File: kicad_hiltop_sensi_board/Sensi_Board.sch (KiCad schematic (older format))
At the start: 98 parts, among them J1 Conn_02x06_Counter_Clockwise, J10 Conn_ARM_JTAG_SWD_10, J2 Conn_02x06_Counter_Clockwise, J3 Conn_03x32_DIN41612, J4 Conn_02x06_Counter_Clockwise, J5 Conn_02x06_Counter_Clockwise, J6 Conn_02x06_Counter_Clockwise, J7 Conn_02x06_Counter_Clockwise, J8 Conn_02x06_Counter_Clockwise, U1 INA250A4, U2 LD1117S33TR_SOT223, U3 AT25DN512CSSHF-B, U6 LM75B

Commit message: Updated sensi board pin map and layout before PCB tracking
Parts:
- C23, C24: Devtank (none) -> 105-019
- J1, J2, J4, J5, J6, J7, J8: Devtank (none) -> 711-004
- J10: Devtank (none) -> 710-020
- JP1: Devtank 710-015 -> 710-014
- R30, R32, R34: Devtank (none) -> 101-005
- R37, R38: Devtank (none) -> 101-010
- R39, R40: Devtank (none) -> 101-015
- R8, R9: Devtank 101-007 -> (none)
- U6: Devtank (none) -> 155-005
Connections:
- net ADC10: no longer J5.3 (Pin_3), TP56.1
- net ADC11: no longer J5.5 (Pin_5), TP57.1
- net ADC12: now also J5.5 (Pin_5), TP57.1; no longer J5.12 (Pin_12), TP58.1
- net ADC6: now also J5.12 (Pin_12), TP58.1
- net ADC7: now also J5.1 (Pin_1), TP55.1
- net ADC9: no longer J5.1 (Pin_1), TP55.1
- net STM_Micro/ADC13 renamed STM_Micro/ADC8
- new net ADC13: J5.3 (Pin_3), TP56.1
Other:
- moved on the sheet: R149
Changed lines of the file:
@@
 F 2 "Connector_PinHeader_2.54mm:PinHeader_1x03_P2.54mm_Vertical" H 18475 3825 50  0001 C CNN
 F 3 "" H 18475 3825 50  0001 C CNN
-F 4 "710-015" H 0   0   50  0001 C CNN "Devtank"
+F 4 "710-014" H 0   0   50  0001 C CNN "Devtank"
 	1    18475 3825
 	0    1    1    0
@@
 F 2 "Resistor_SMD:R_1206_3216Metric" V 17755 9150 50  0001 C CNN
 F 3 "" H 17825 9150 50  0001 C CNN
-F 4 "101-007" H -350 1050 50  0001 C CNN "Devtank"
+F 4 "" H -350 1050 50  0001 C CNN "Devtank"
 	1    17825 9150
 	-1   0    0    1
@@
 F 2 "Resistor_SMD:R_1206_3216Metric" V 17505 9150 50  0001 C CNN
 F 3 "" H 17575 9150 50  0001 C CNN
-F 4 "101-007" H -350 1050 50  0001 C CNN "Devtank"
+F 4 "" H -350 1050 50  0001 C CNN "Devtank"
 	1    17575 9150
 	-1   0    0    1
@@
 Wire Wire Line
 	3225 3725 2175 3725
-Wire Wire Line
-	3225 3850 2175 3850
 Text Label 2175 2975 0    60   ~ 0
 ADC1
@@
 Text Label 2175 3725 0    60   ~ 0
 ADC7
-Text Label 2175 3850 0    60   ~ 0
-ADC8
 Text Label 2175 3975 0    60   ~ 0
 ADC9
@@
 Wire Wire Line
 	21675 5250 21675 5175
-Text Label 950  4475 0    60   ~ 0
+Text Label 950  3850 0    60   ~ 0
 I_MON
 Text Label 20800 11050 2    60   ~ 0
@@
 L Sensi_Board-rescue:R-device R149
 U 1 1 5CC4B709
-P 1875 4475
-F 0 "R149" V 1825 4225 50  0000 C CNN
-F 1 "0R" V 1825 4700 50  0000 C CNN
-F 2 "Resistor_SMD:R_0603_1608Metric" V 1805 4475 50  0001 C CNN
-F 3 "" H 1875 4475 50  0001 C CNN
-F 4 "101-005" H 150 1150 50  0001 C CNN "Devtank"
-	1    1875 4475
+P 1875 3850
+F 0 "R149" V 1825 3600 50  0000 C CNN
+F 1 "0R" V 1825 4075 50  0000 C CNN
+F 2 "Resistor_SMD:R_0603_1608Metric" V 1805 3850 50  0001 C CNN
+F 3 "" H 1875 3850 50  0001 C CNN
+F 4 "101-005" H 150 525 50  0001 C CNN "Devtank"
+	1    1875 3850
 	0    1    1    0
 $EndComp
 Wire Wire Line
-	950  4475 1725 4475
+	950  3850 1725 3850
 Wire Wire Line
 	2175 3475 3225 3475
@@
 ADC12
 Wire Wire Line
-	2025 4475 3225 4475
+	2025 3850 3225 3850
 Text Label 13850 4525 0    60   ~ 0
 USB_DATA_N
@@
 Wire Wire Line
 	12525 7775 13025 7775
-Text Label 13025 7775 2    60   ~ 0
+Text Label 13025 6875 2    60   ~ 0
 ADC5
-Text Label 13025 7475 2    60   ~ 0
+Text Label 11025 14750 2    60   ~ 0
 ADC6
-Text Label 13025 7175 2    60   ~ 0
+Text Label 11025 14300 2    60   ~ 0
 ADC7
-Text Label 13025 6875 2    60   ~ 0
-ADC8
+Text Label 11050 14450 2    60   ~ 0
+ADC13
 Wire Wire Line
 	20900 5250 20425 5250
@@
 	20425 5150 20425 5250
 Connection ~ 20425 5250
-Text Label 8350 9450 2    60   ~ 0
+Text Label 13025 7175 2    60   ~ 0
 ADC4
-Text Label 8350 8850 2    60   ~ 0
+Text Label 13025 7475 2    60   ~ 0
 ADC3
-Text Label 8350 8550 2    60   ~ 0
+Text Label 13025 7775 2    60   ~ 0
 ADC2
 Text Label 8350 9150 2    60   ~ 0
@@
 Text Label 8675 14750 0    60   ~ 0
 5V_ADC12
-Text Label 11100 14750 2    60   ~ 0
+Text Label 11050 14600 2    60   ~ 0
 ADC12
 $Comp
@@
 F 2 "Package_SO:SOIC-8_3.9x4.9mm_P1.27mm" H 8300 11650 50  0001 C CNN
 F 3 "http://www.ti.com/lit/ds/symlink/lm75b.pdf" H 8300 11650 50  0001 C CNN
+F 4 "155-005" H 8300 11650 50  0001 C CNN "Devtank"
 	1    8300 11650
 	-1   0    0    -1
@@
 F 2 "Capacitor_SMD:C_0402_1005Metric" H 8738 10825 50  0001 C CNN
 F 3 "" H 8700 10975 50  0001 C CNN
+F 4 "105-019" H 8700 10975 50  0001 C CNN "Devtank"
 	1    8700 10975
 	0    -1   -1   0
@@
 F 2 "Resistor_SMD:R_0603_1608Metric" V 7305 11275 50  0001 C CNN
 F 3 "" H 7375 11275 50  0001 C CNN
+F 4 "101-005" H 7375 11275 50  0001 C CNN "Devtank"
 	1    7375 11275
 	1    0    0    -1
@@
 F 2 "Resistor_SMD:R_0603_1608Metric" V 7555 11275 50  0001 C CNN
 F 3 "" H 7625 11275 50  0001 C CNN
+F 4 "101-005" H 7625 11275 50  0001 C CNN "Devtank"
 	1    7625 11275
 	1    0    0    -1
@@
 F 2 "Resistor_SMD:R_0603_1608Metric" V 7055 11275 50  0001 C CNN
 F 3 "" H 7125 11275 50  0001 C CNN
+F 4 "101-005" H 7125 11275 50  0001 C CNN "Devtank"
 	1    7125 11275
 	1    0    0    -1
@@
 F 2 "Resistor_SMD:R_0603_1608Metric" V 5480 11300 50  0001 C CNN
 F 3 "" H 5550 11300 50  0001 C CNN
+F 4 "101-010" H 5550 11300 50  0001 C CNN "Devtank"
 	1    5550 11300
 	0    1    1    0
@@
 F 2 "Resistor_SMD:R_0603_1608Metric" V 5280 10650 50  0001 C CNN
 F 3 "" H 5350 10650 50  0001 C CNN
+F 4 "101-010" H 5350 10650 50  0001 C CNN "Devtank"
 	1    5350 10650
 	1    0    0    -1
@@
 F 2 "Connector_PinHeader_2.54mm:PinHeader_2x05_P2.54mm_Vertical" H 1750 7950 50  0001 L TNN
 F 3 "http://infocenter.arm.com/help/topic/com.arm.doc.faqs/attached/13634/cortex_debug_connectors.pdf" V 1350 7250 50  0001 C CNN
+F 4 "710-020" H 1700 8500 50  0001 C CNN "Devtank"
 	1    1700 8500
 	1    0    0    -1
@@
 F 2 "Capacitor_SMD:C_0402_1005Metric" H 988 8300 50  0001 C CNN
 F 3 "" H 950 8450 50  0001 C CNN
+F 4 "105-019" H 950 8450 50  0001 C CNN "Devtank"
 	1    950  8450
 	1    0    0    -1
@@
 F 2 "Resistor_SMD:R_0603_1608Metric" V 2880 8400 50  0001 C CNN
 F 3 "" H 2950 8400 50  0001 C CNN
+F 4 "101-015" H 2950 8400 50  0001 C CNN "Devtank"
 	1    2950 8400
 	0    -1   -1   0
@@
 F 2 "Resistor_SMD:R_0603_1608Metric" V 2880 8550 50  0001 C CNN
 F 3 "" H 2950 8550 50  0001 C CNN
+F 4 "101-015" H 2950 8550 50  0001 C CNN "Devtank"
 	1    2950 8550
 	0    -1   -1   0
@@
 F 2 "Devtank_PCB_Lib:Molex2x06" H 12750 10075 50  0001 C CNN
 F 3 "~" H 12750 10075 50  0001 C CNN
+F 4 "711-004" H 12750 10075 50  0001 C CNN "Devtank"
 	1    12750 10075
 	1    0    0    -1
@@
 F 2 "Devtank_PCB_Lib:Molex2x06" H 12725 11375 50  0001 C CNN
 F 3 "~" H 12725 11375 50  0001 C CNN
+F 4 "711-004" H 12725 11375 50  0001 C CNN "Devtank"
 	1    12725 11375
 	1    0    0    -1
@@
 F 2 "Devtank_PCB_Lib:Molex2x06" H 7150 14425 50  0001 C CNN
 F 3 "~" H 7150 14425 50  0001 C CNN
+F 4 "711-004" H 7150 14425 50  0001 C CNN "Devtank"
 	1    7150 14425
 	1    0    0    -1
@@
 	6950 14225 6525 14225
 Text Label 6525 14225 0    60   ~ 0
-ADC9
+ADC7
 Wire Wire Line
 	6950 14425 6525 14425
 Text Label 6525 14425 0    60   ~ 0
-ADC10
+ADC13
 Wire Wire Line
 	6950 14625 6525 14625
 Text Label 6525 14625 0    60   ~ 0
-ADC11
+ADC12
 Wire Wire Line
 	7450 14225 7875 14225
 Text Label 7875 14225 2    60   ~ 0
-ADC12
+ADC6
 NoConn ~ 7450 14525
 NoConn ~ 7450 14425
@@
 F 2 "Devtank_PCB_Lib:Molex2x06" H 10000 7300 50  0001 C CNN
 F 3 "~" H 10000 7300 50  0001 C CNN
+F 4 "711-004" H 10000 7300 50  0001 C CNN "Devtank"
 	1    10000 7300
 	1    0    0    -1
@@
 F 2 "Devtank_PCB_Lib:Molex2x06" H 4925 8950 50  0001 C CNN
 F 3 "~" H 4925 8950 50  0001 C CNN
+F 4 "711-004" H 4925 8950 50  0001 C CNN "Devtank"
 	1    4925 8950
 	1    0    0    -1
@@
 F 2 "Devtank_PCB_Lib:Molex2x06" H 4700 11200 50  0001 C CNN
 F 3 "~" H 4700 11200 50  0001 C CNN
+F 4 "711-004" H 4700 11200 50  0001 C CNN "Devtank"
 	1    4700 11200
 	1    0    0    -1
@@
 F 2 "Devtank_PCB_Lib:Molex2x06" H 1950 11325 50  0001 C CNN
 F 3 "~" H 1950 11325 50  0001 C CNN
+F 4 "711-004" H 1950 11325 50  0001 C CNN "Devtank"
 	1    1950 11325
 	1    0    0    -1
@@
 NoConn ~ 7450 14625
 NoConn ~ 7450 14725
-Text Label 11100 14600 2    60   ~ 0
+Text Label 8350 8550 2    60   ~ 0
 ADC11
-Text Label 11100 14450 2    60   ~ 0
+Text Label 8350 8850 2    60   ~ 0
 ADC10
-Text Label 11100 14300 2    60   ~ 0
+Text Label 8350 9450 2    60   ~ 0
 ADC9
 Wire Wire Line
@@
 NoConn ~ 2525 6775
 NoConn ~ 2525 6900
+Wire Wire Line
+	3225 4475 2175 4475
+Text Label 2175 4475 0    60   ~ 0
+ADC13
 $EndSCHEMATC

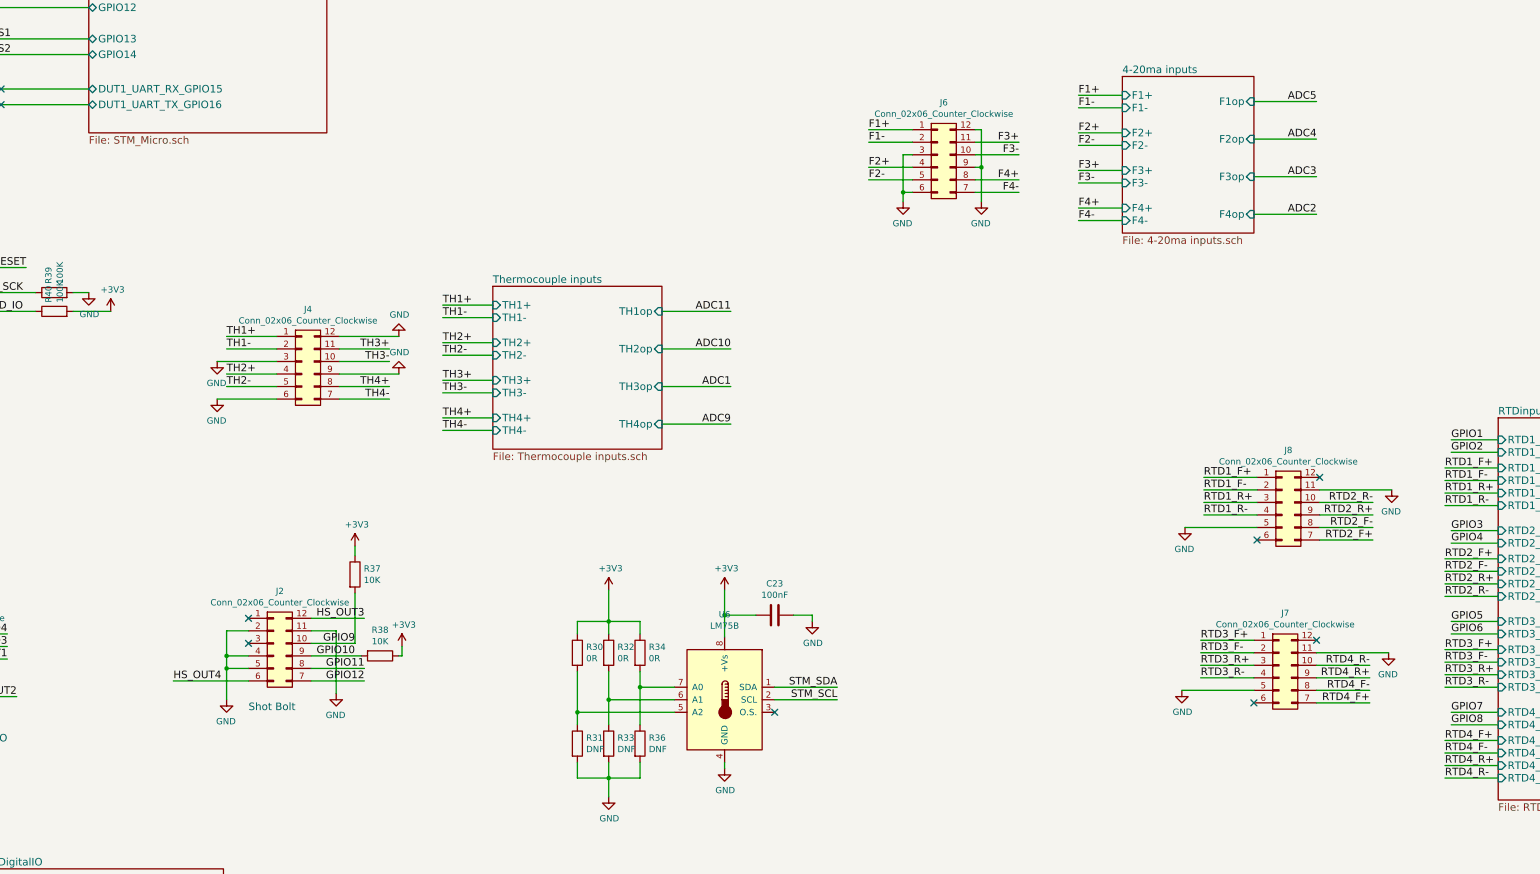
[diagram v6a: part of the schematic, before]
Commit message: Started PCB routing of Sensi Board LBBC
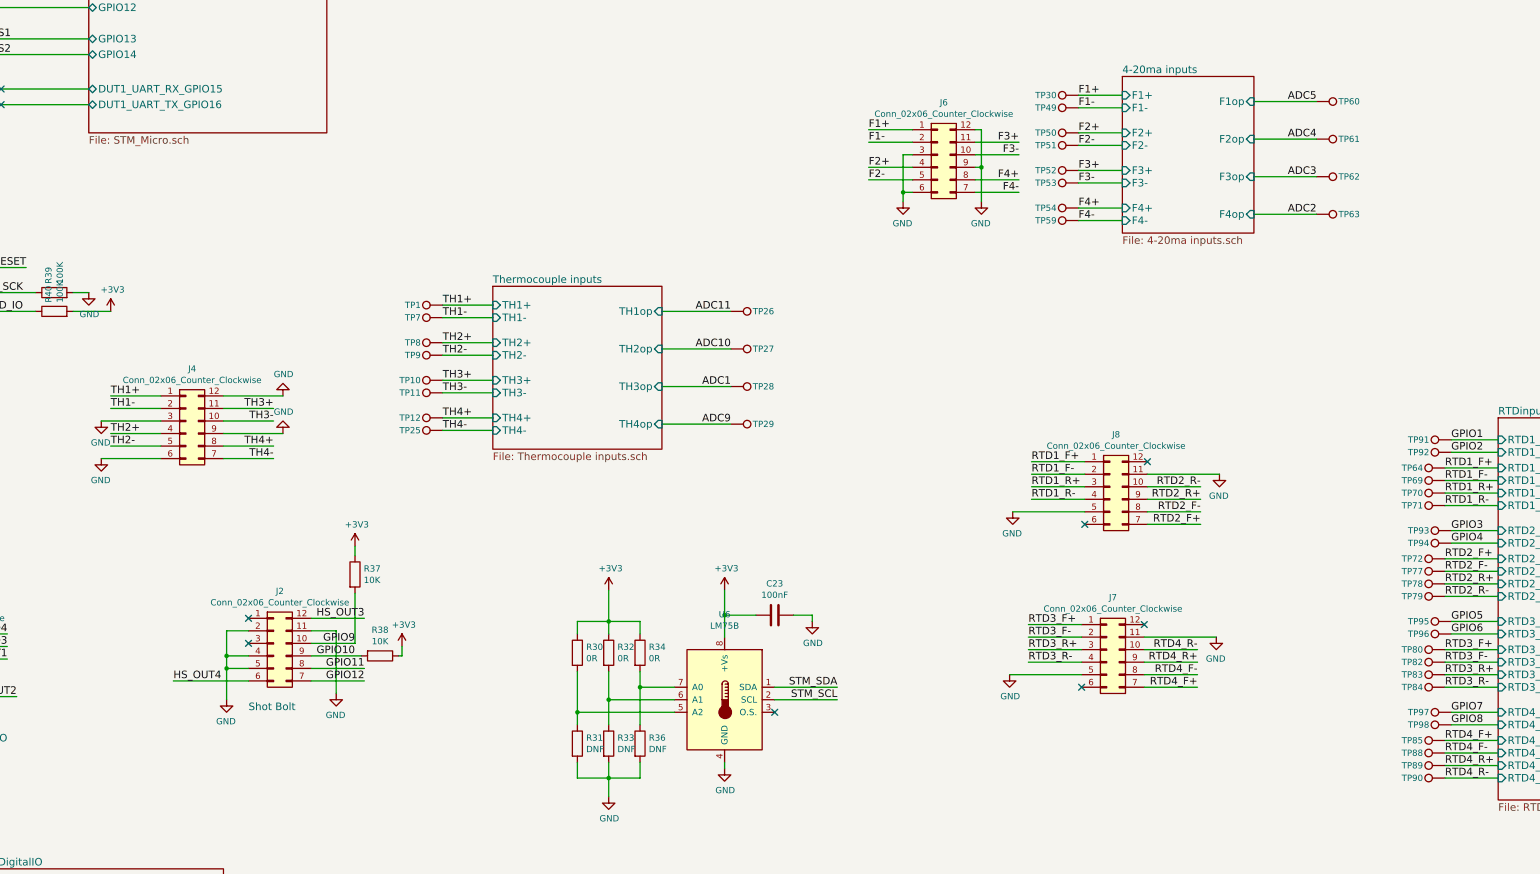
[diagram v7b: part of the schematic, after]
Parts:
- added TP1, TP10, TP11, TP12, TP25, TP26, TP27, TP28, TP29, TP30, TP49, TP50, TP51, TP52, TP53, TP54, TP59, TP60, TP61, TP62, TP63, TP64, TP69, TP7, TP70, TP71, TP72, TP77, TP78, TP79, TP8, TP80, TP82, TP83, TP84, TP85, TP88, TP89, TP9, TP90, TP91, TP92, TP93, TP94, TP95, TP96, TP97, TP98: Test_Point, TestPoint:TestPoint_THTPad_D1.0mm_Drill0.5mm, symbol Sensi_Board-rescue:Test_Point-Connector
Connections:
- net ADC1: now also TP28.1
- net ADC10: now also TP27.1
- net ADC11: now also TP26.1
- net ADC2: now also TP63.1
- net ADC3: now also TP62.1
- net ADC4: now also TP61.1
- net ADC5: now also TP60.1
- net ADC9: now also TP29.1
- net F1+: now also TP30.1
- net F1-: now also TP49.1
- net F2+: now also TP50.1
- net F2-: now also TP51.1
- net F3+: now also TP52.1
- net F3-: now also TP53.1
- net F4+: now also TP54.1
- net F4-: now also TP59.1
- net GPIO1: now also TP91.1
- net GPIO2: now also TP92.1
- net GPIO3: now also TP93.1
- net GPIO4: now also TP94.1
- net GPIO5: now also TP95.1
- net GPIO6: now also TP96.1
- net GPIO7: now also TP97.1
- net GPIO8: now also TP98.1
- net RTD1_F+: now also TP64.1
- net RTD1_F-: now also TP69.1
- net RTD1_R+: now also TP70.1
- net RTD1_R-: now also TP71.1
- net RTD2_F+: now also TP72.1
- net RTD2_F-: now also TP77.1
- net RTD2_R+: now also TP78.1
- net RTD2_R-: now also TP79.1
- net RTD3_F+: now also TP80.1
- net RTD3_F-: now also TP82.1
- net RTD3_R+: now also TP83.1
- net RTD3_R-: now also TP84.1
- net RTD4_F+: now also TP85.1
- net RTD4_F-: now also TP88.1
- net RTD4_R+: now also TP89.1
- net RTD4_R-: now also TP90.1
- net TH1+: now also TP1.1
- net TH1-: now also TP7.1
- net TH2+: now also TP8.1
- net TH2-: now also TP9.1
- net TH3+: now also TP10.1
- net TH3-: now also TP11.1
- net TH4+: now also TP12.1
- net TH4-: now also TP25.1
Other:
- moved on the sheet: J4, J7, J8

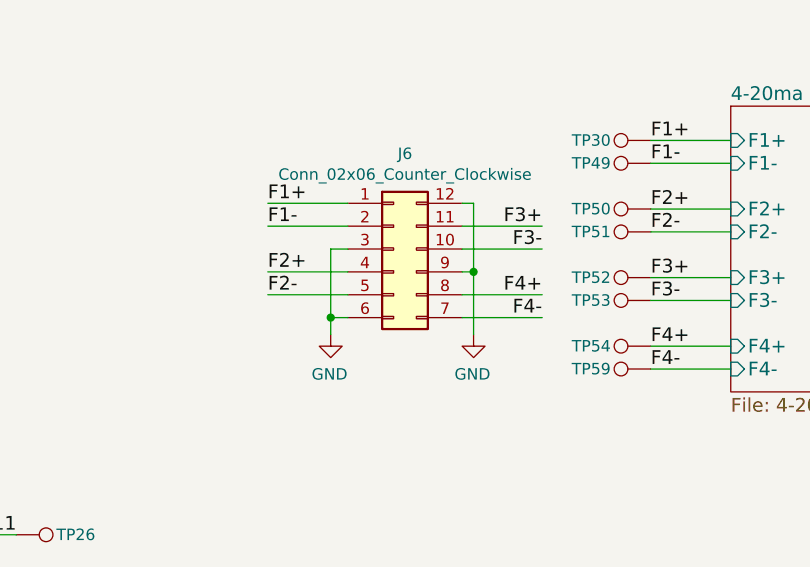
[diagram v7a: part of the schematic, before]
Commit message: Routing complete around the chip of sensi board
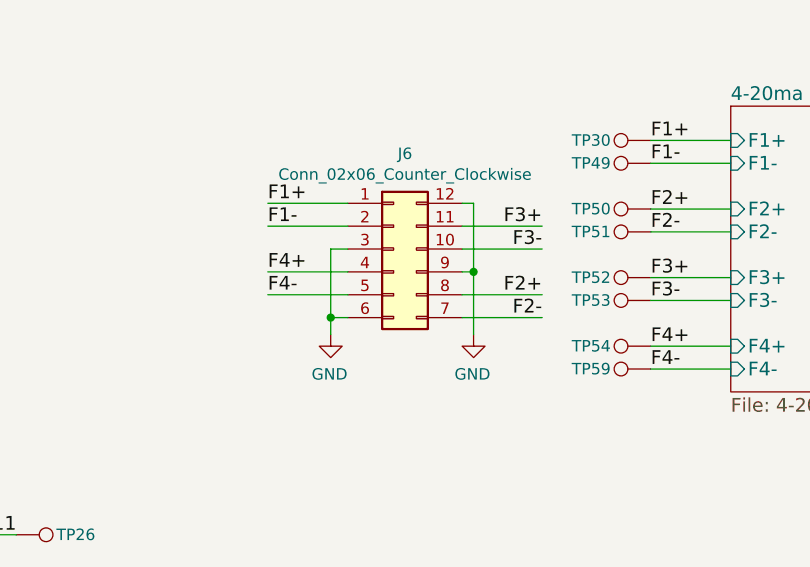
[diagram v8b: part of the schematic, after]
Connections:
- net F2+: now also J6.8 (Pin_8); no longer J6.4 (Pin_4)
- net F2-: now also J6.7 (Pin_7); no longer J6.5 (Pin_5)
- net F4+: now also J6.4 (Pin_4); no longer J6.8 (Pin_8)
- net F4-: now also J6.5 (Pin_5); no longer J6.7 (Pin_7)
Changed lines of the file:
@@
 Wire Wire Line
 	10300 7600 10650 7600
-Text Label 10650 7500 2    60   ~ 0
+Text Label 9450 7400 0    60   ~ 0
 F4+
-Text Label 10650 7600 2    60   ~ 0
+Text Label 9450 7500 0    60   ~ 0
 F4-
 $Comp
@@
 	1    0    0    -1
 $EndComp
-Text Label 9450 7500 0    60   ~ 0
+Text Label 10650 7600 2    60   ~ 0
 F2-
-Text Label 9450 7400 0    60   ~ 0
+Text Label 10650 7500 2    60   ~ 0
 F2+
 Wire Wire Line
